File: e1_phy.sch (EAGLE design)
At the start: 136 parts, among them IC2 LD117AS33TR, IC3 LD117AS33TR, IC4 MCP4725, U1 XRT82D20, U2 GPS_GNS_2201, U3 VCTCXO-CONNORWINFIELD, U4 VCXO_TAITIEN_VT, X2 SMA-142-0701-801/806, X3 JACK2.5_SJ-2523, X4 0446200002

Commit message: Changed LIU to IDT82V2081.
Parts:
- removed LED1, LED2: (no value), led:LEDCHIPLED_0603
- removed R16, R17: 0R, rcl:R-EU_R0603
- removed R18, R19, R20, R24: DNP, rcl:R-EU_R0603
- removed R21, R22, R23, R29, R54, R55: 1k, rcl:R-EU_R0603
- removed SV4: (no value), con-lstb:MA08-2
- removed TP1, TP17, TP2, TP3, TP4, TP5, TP6: TPB1,27, testpad:TPB1,27
- added C29: 100n, rcl:C-EUC0603
- added D2, D3, D4, D5, D6, D7, D8, D9: MBR0520LT, diode:MBR0520LT
- added U$2: MNR 8x10k, laforge:MNR
- C3: value 10u -> 100n
- R10, R11: value 9R1 -> 10k
- R12: value DNP -> 10k
- R8: value 60R -> DNP
- R9: value 60R -> 3k 1%
- TR1: value PE-65861 -> PULSE_T1094NL; device cvogel:PULSE_PE65861 -> laforge:PULSE_T1094NL
- U1: value XRT82D20 -> IDT82V2081; device cvogel:XRT82D20 -> idt82v2081:IDT82V2081
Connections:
- removed net #ATM: R24.1, U1.#ATM
- removed net #CLKLOS: R23.1, SV4.8, U$1.PA8_XOUT32, U1.#CLKLOS
- removed net #DLOOP: SV4.10, U1.#DLOOP
- removed net #LLOOP: SV4.12, U1.#LLOOP
- removed net #RLOOP: SV4.11, U1.#RLOOP
- removed net #RLOS: R22.1, SV4.7, U$1.PA7_XIN32, U1.#RLOS
- removed net DIGI: R18.1, U1.DIGI
- removed net JAEN: R54.2, SV4.14, U1.JAEN
- removed net JATX: R55.2, SV4.13, U1.JATX_DR
- removed net MUTERX: R21.1, U1.MUTERX
- removed net N$1: LED1.C, R22.2
- removed net N$2: LED2.C, R23.2
- removed net RAOS: R19.2, U1.RAOS
- removed net RRING_LIU: R17.2, TP2.TP, U1.RRING
- removed net RTIP_LIU: R16.2, TP1.TP, U1.RTIP
- removed net RX_PRI_CTR: R1.2, TR1A.PRI_2
- removed net RX_VIOLATION: SV4.4, U1.RNEG_LCV
- removed net TAOS: R20.2, U1.TAOS
- removed net TNEG_CODE: R29.1, SV4.9, U1.TNEG_CODE
- removed net TRING_XFMR: R11.1, TR1B.PRI_3
- removed net TTIP_XFMR: R10.1, TR1B.PRI_1
- removed net TX_PRI_CTR: R12.1, TR1B.PRI_2
- removed net TX_SEC_CTR: R2.2, TR1B.SEC_2
- new net #RST_LIU: U$1.PA8_XOUT32, U1.#RST
- new net #SPI_CS2: R11.1, SV6.6, U$1.PA30
- new net AD0: U$2.8, U1.AD0_PATT0
- new net AD1: U$2.4, U1.AD1/PATT1
- new net AD2: U$2.7, U1.AD2/RPD
- new net AD3: U$2.3, U1.AD3/EQ
- new net AD4: U$2.6, U1.AD4/PULS0
- new net AD5: U$2.2, U1.AD5/PULS1
- new net AD6: U$2.5, U1.AD6/PULS2
- new net AD7: U$2.1, U1.AD7/PULS3
- new net LOS_LIU: U$1.PA7_XIN32, U1.LOS
- new net N$25: R8.2, TR1-1:2.P$6
- new net N$31: R9.1, U1.R_REF
- net #SPI_CS0: now also R10.1
- net #SPI_CS1: now also R12.2, U$1.PA31, U1.#CS/RXTX1; no longer SV6.6, U$1.PA30
- net +UB: now also C29.1, U1.VDDA
- net CLK2048: no longer SV4.16
- net E1_LINE_RX_A: now also TR1-1:1.P$1; no longer TR1A.PRI_1
- net E1_LINE_RX_B: now also TR1-1:1.P$3; no longer TR1A.PRI_3
- net E1_LINE_TX_A: now also TR1-1:2.P$1; no longer TR1B.SEC_1
- net E1_LINE_TX_B: now also TR1-1:2.P$3; no longer TR1B.SEC_3
- net GND: now also C29.2, D6.A, D7.A, D8.A, D9.A, U$2.C, U$2.D, U1.GNDA, U1.GNDD, U1.GNDIO, U1.GNDT, U1.IC2_GND, U1.JA0, U1.JA1, U1.MODE1, U1.RCLKE, U1.SCLKE/#RD/#DS/MONT, U1.TDN, U1.THZ; no longer R12.2, R24.2, R8.2, SV4.15, SV4.2, TP5.TP, TR1A.SEC_2, U1.AGND, U1.TGND, U1.TXLEV
- net GNDIO: no longer R1.1, R2.1, TP6.TP
- net N$5: now also R2.2, TR1-1:2.P$4; no longer TP17.TP, U$1.PA31
- net RRING: now also D3.A, D7.C, R1.2, TR1-1:1.P$6, U1.RRING; no longer R17.1, R9.1, TR1A.SEC_3
- net RTIP: now also D2.A, D6.C, R1.1, TR1-1:1.P$4, U1.RTIP; no longer R16.1, R8.1, TR1A.SEC_1
- net RX_CLK: no longer SV4.3
- net RX_DATA: now also U1.RD_RDP; no longer SV4.1, U1.RPOS_RDATA
- net SPI_MISO: now also U1.SDO/#ACK/RDY/TERM
- net SPI_MOSI: now also U1.SDI/#WR/R#W/LP0
- net SPI_SCK: now also U1.SCLK/ALE/AS/LP1
- net TRING: now also D5.A, D9.C, R8.1; no longer R11.2, TP4.TP
- net TTIP: now also D4.A, D8.C, R2.1; no longer R10.2, TP3.TP
- net TX_CLK: no longer SV4.5
- net TX_DATA: now also U1.TD_TDP; no longer SV4.6, U1.TPOS_TDATA
- net VCC: now also D2.C, D3.C, D4.C, D5.C, R10.2, R11.2, R12.1, U1.MODE0, U1.VDDD, U1.VDDIO, U1.VDDT; no longer LED1.A, LED2.A, R18.2, R19.1, R20.1, R21.2, R29.2, R54.1, R55.1, U1.AVDD, U1.TVDD
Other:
- note added: "1"
- note added: "16-14=PRI PRI:SEC=1:1"
- note added: "2"
- note added: "6-8=PRI PRI:SEC=1:2"
- note added: "e1_sam4_usb vogelchr@vogel.cx 2018-06-25 for review"
- note removed: "JAEN&JATX int pd ext pu to enable and put in TX path RAOS int pd: disable receive all ones TAOS int pd: disable transmit all ones"
- note removed: "LUI Signals"
- note removed: "Line:LIU Rx 1:2"
- note removed: "Line:LIU Tx 2:1"
- note removed: "MuteRX ext pullup: enable #ClkLOS=0 RCLK=1, RDATA=0 DIGI: int. pulldn: xDATA high active TNEG ext pullup: int. HDB3 enc/decoder #ATM int pullup: alarm test mode inactive"
- note removed: "e1_sam4_usb vogelchr@vogel.cx 2018-06-24 for review"
- note removed: "line side R should probably *never* be populated!"
- moved on the sheet: C1, C2, C3, R1, R10, R11, R12, R2, R8, R9

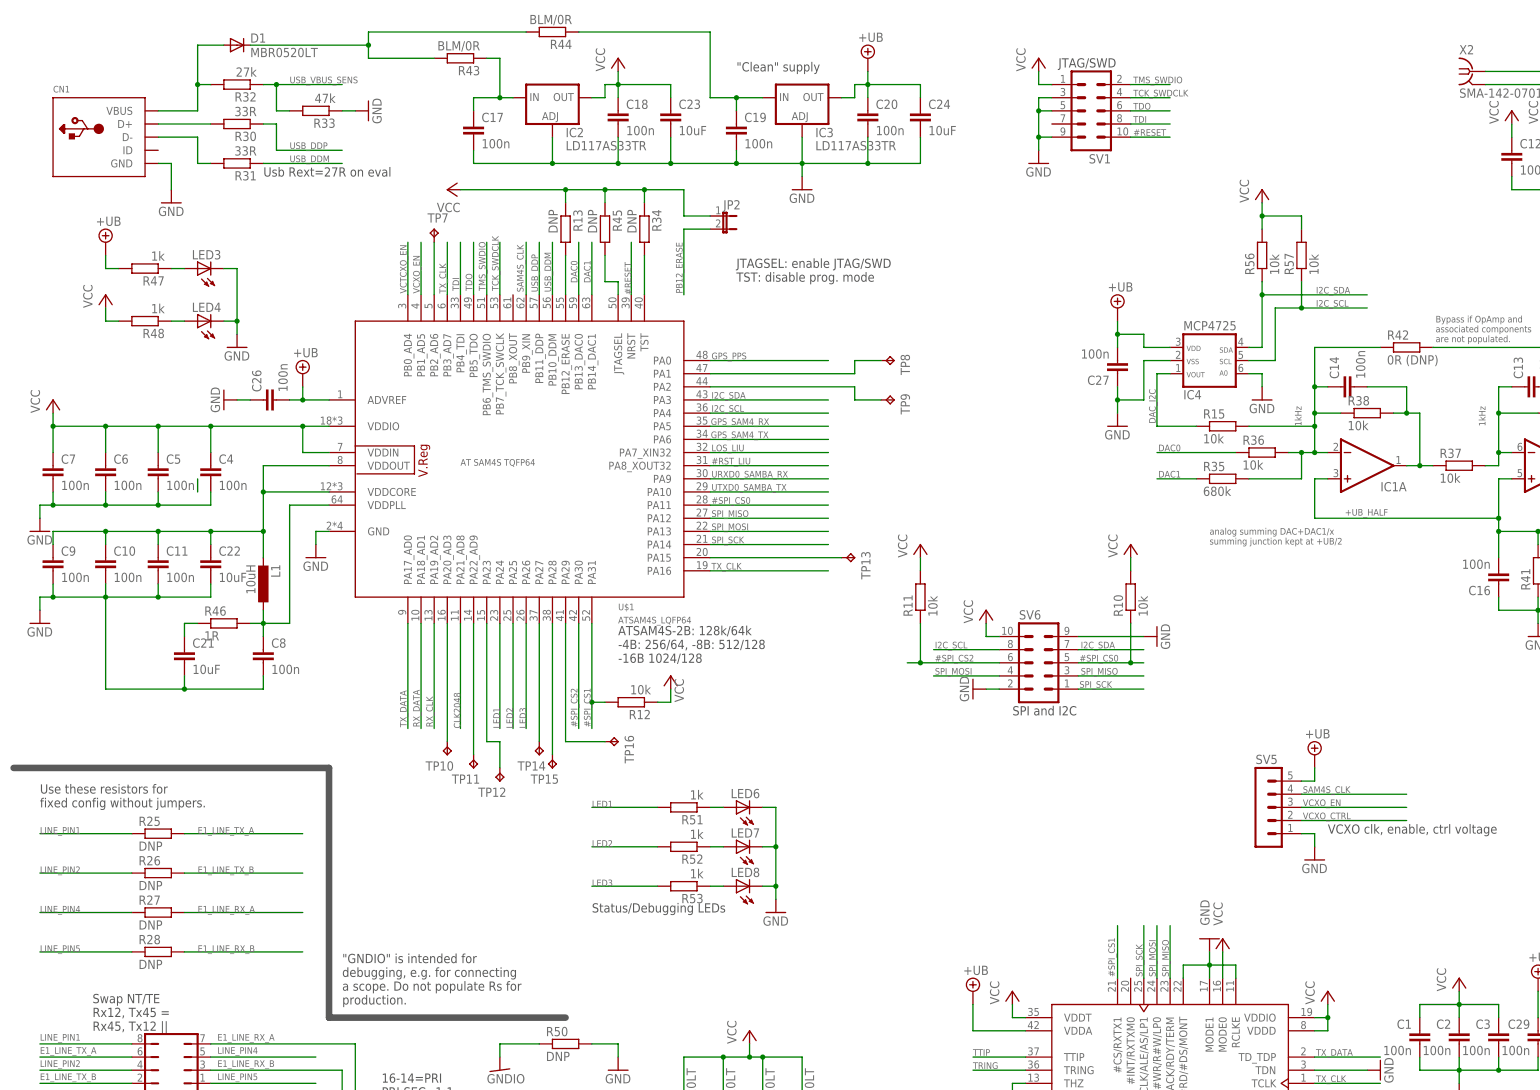
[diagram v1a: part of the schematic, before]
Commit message: Implement review: ESD protection on USB.
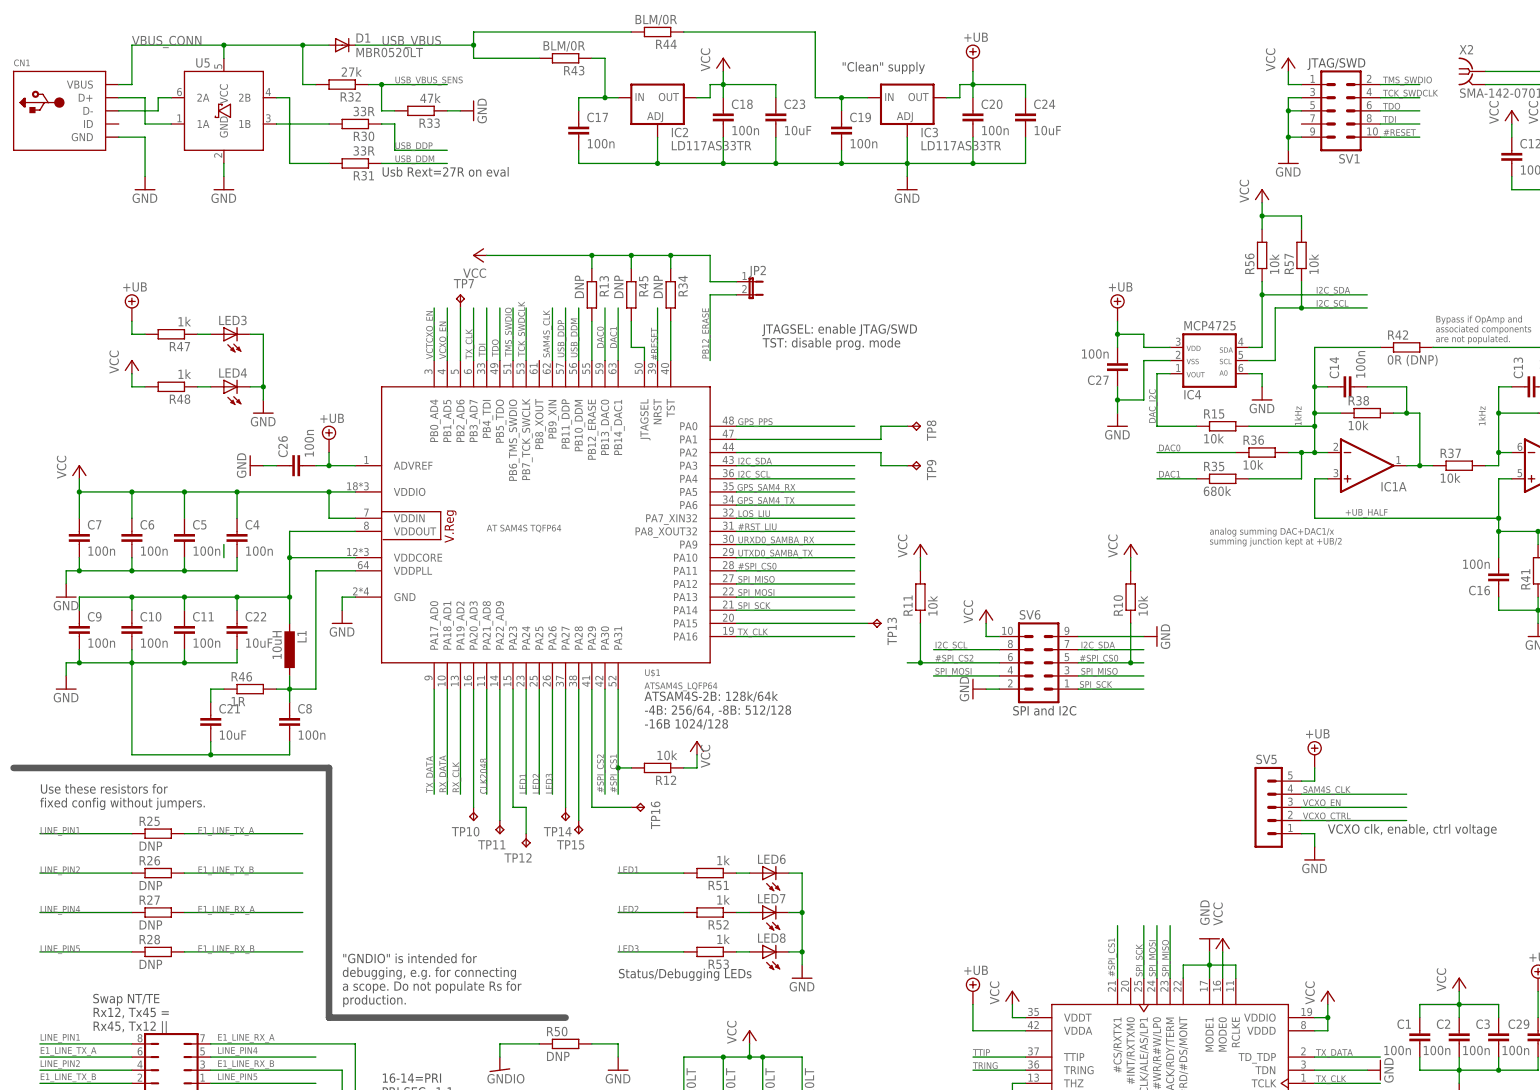
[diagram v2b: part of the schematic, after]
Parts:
- added U5: IP4234CZ6, laforge:IP4234CZ6
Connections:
- net USB_VBUS_CON renamed USB_VBUS
- removed net N$12: CN1.VBUS, D1.A, R32.2
- new net N$1: CN1.D+, U5.1A
- new net N$2: CN1.D-, U5.2A
- new net VBUS_CONN: CN1.VBUS, D1.A, R32.2, U5.VCC
- net GND: now also U5.GND
- net USB_DDM_CON: now also U5.2B; no longer CN1.D-
- net USB_DDP_CON: now also U5.1B; no longer CN1.D+
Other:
- moved on the sheet: C10, C11, C17, C18, C19, C20, C21, C22, C23, C24, C26, C4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

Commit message: Implement review comment: R1 120 Ohms, R2, R2 9 Ohs
Termination on Rx input and output impedance on Tx.
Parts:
- R1: value DNP -> 120R
- R2, R8: value DNP -> 9R
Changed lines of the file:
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@@
 <part name="GND9" library="supply1" deviceset="GND" device=""/>
 <part name="TR1" library="laforge" deviceset="PULSE_T1094NL" device=""/>
-<part name="R1" library="rcl" deviceset="R-EU_" device="R0603" value="DNP"/>
-<part name="R2" library="rcl" deviceset="R-EU_" device="R0603" value="DNP"/>
-<part name="R8" library="rcl" deviceset="R-EU_" device="R0603" value="DNP"/>
+<part name="R1" library="rcl" deviceset="R-EU_" device="R0603" value="120R"/>
+<part name="R2" library="rcl" deviceset="R-EU_" device="R0603" value="9R"/>
+<part name="R8" library="rcl" deviceset="R-EU_" device="R0603" value="9R"/>
 <part name="GND10" library="supply1" deviceset="GND" device=""/>
 <part name="R9" library="rcl" deviceset="R-EU_" device="R0603" value="3k 1%"/>

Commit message: Implement review comment: LIU move signal from LOS to #INT
 - LIU move signal from LOS to #INT
   -> Interrupt can be generated on LOS anyway.
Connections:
- removed net LOS_LIU: U$1.PA7_XIN32, U1.LOS
- new net #LIU_INT: U$1.PA7_XIN32, U1.#INT/RXTXM0
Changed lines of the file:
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@@
-</segment>
-</net>
-<net name="LOS_LIU" class="0">
-<segment>
-<pinref part="U$1" gate="G$1" pin="PA7_XIN32"/>
-<wire x1="142.24" y1="165.1" x2="165.1" y2="165.1" width="0.1524" layer="91"/>
-<label x="142.494" y="165.354" size="1.27" layer="95"/>
-</segment>
-<segment>
-<pinref part="U1" gate="G$1" pin="LOS"/>
-<wire x1="254" y1="35.56" x2="266.7" y2="35.56" width="0.1524" layer="91"/>
-<label x="254.254" y="35.814" size="1.27" layer="95"/>
 </segment>
 </net>
@@
 </segment>
 </net>
+<net name="#LIU_INT" class="0">
+<segment>
+<pinref part="U1" gate="G$1" pin="#INT/RXTXM0"/>
+<wire x1="218.44" y1="76.2" x2="218.44" y2="86.36" width="0.1524" layer="91"/>
+<label x="218.186" y="76.454" size="1.27" layer="95" rot="R90"/>
+</segment>
+<segment>
+<pinref part="U$1" gate="G$1" pin="PA7_XIN32"/>
+<wire x1="142.24" y1="165.1" x2="165.1" y2="165.1" width="0.1524" layer="91"/>
+<label x="142.494" y="165.354" size="1.27" layer="95"/>
+</segment>
+</net>
